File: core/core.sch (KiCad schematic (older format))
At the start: 53 parts, among them J1 Micro_SD_Card, J2 UART_DEBUG, J3 Conn_ARM_JTAG_SWD_10, J4 Conn_01x02, J5 USB_OTG, SW1 RESET, SW2 USER, U1 SC18IS600, U2 AP1509-50, U3 AP1509-33, U4 USBLC6-2SC6

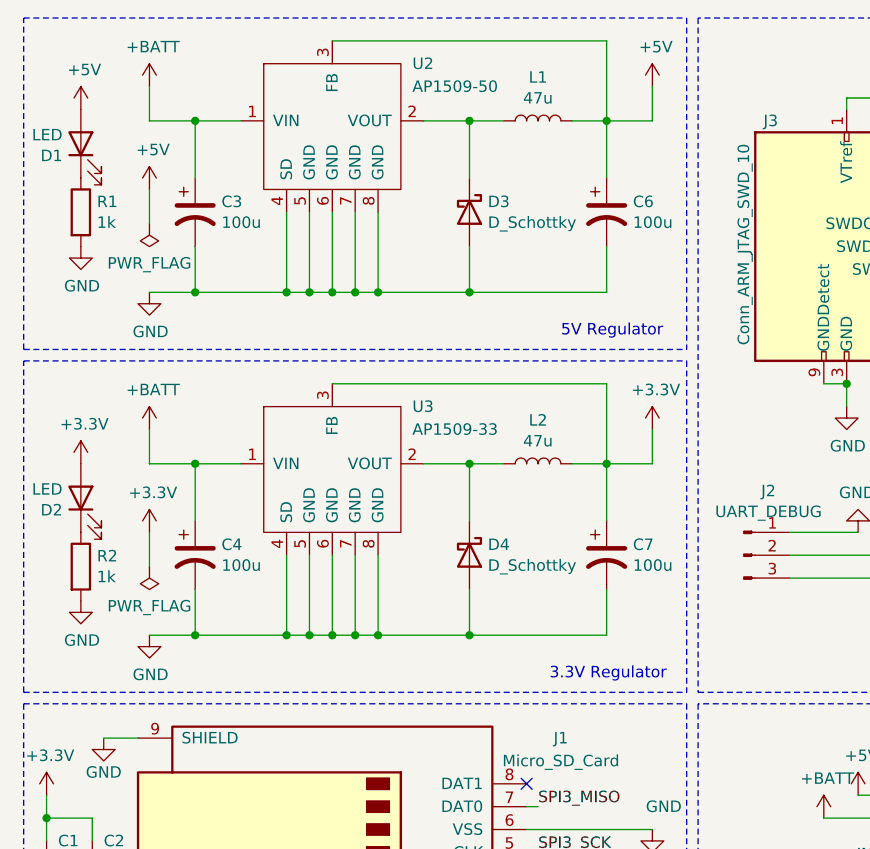
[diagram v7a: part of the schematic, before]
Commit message: New regulator
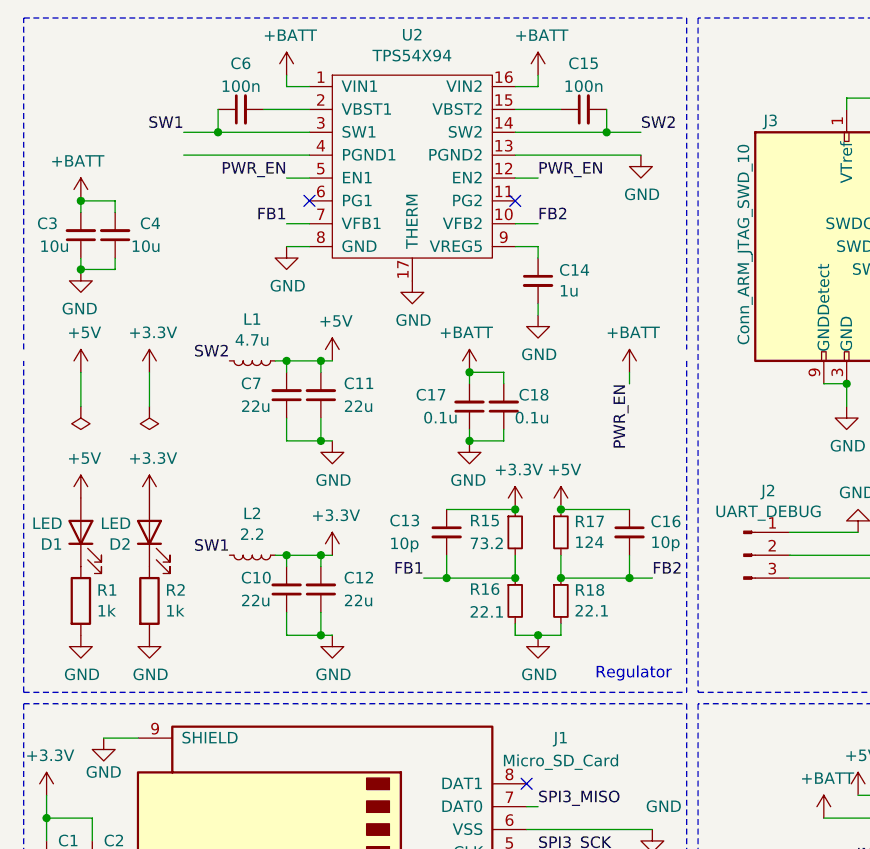
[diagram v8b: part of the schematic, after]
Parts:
- removed C3, C4, C6, C7: 100u, Capacitor_SMD:C_1210_3225Metric, symbol Device:CP1
- removed D3, D4: D_Schottky, Diode_SMD:D_0603_1608Metric, symbol Device:D_Schottky
- removed L1, L2: 47u, Inductor_SMD:L_Bourns-SRN8040_8x8.15mm, symbol Device:L
- removed U2: AP1509-50, Package_SO:SO-8_3.9x4.9mm_P1.27mm, symbol star-common-lib:AP1509-33
- removed U3: AP1509-33, Package_SO:SO-8_3.9x4.9mm_P1.27mm, symbol star-common-lib:AP1509-33
- added C10, C11, C12, C7: 22u, Capacitor_SMD:C_1206_3216Metric, symbol Device:C_Small
- added C13, C16: 10p, Capacitor_SMD:C_1206_3216Metric, symbol Device:C_Small
- added C14: 1u, Capacitor_SMD:C_1206_3216Metric, symbol Device:C_Small
- added C15, C6: 100n, Capacitor_SMD:C_1206_3216Metric, symbol Device:C_Small
- added C17, C18: 0.1u, Capacitor_SMD:C_0603_1608Metric, symbol Device:C_Small
- added C3, C4: 10u, Capacitor_SMD:C_0603_1608Metric, symbol Device:C_Small
- added L1: 4.7u, Inductor_SMD:L_Bourns_SRP5030T, symbol Device:L_Small
- added L2: 2.2, Inductor_SMD:L_Bourns_SRP5030T, symbol Device:L_Small
- added R15: 73.2, Resistor_SMD:R_0603_1608Metric, symbol Device:R_Small
- added R16, R18: 22.1, Resistor_SMD:R_0603_1608Metric, symbol Device:R_Small
- added R17: 124, Resistor_SMD:R_0603_1608Metric, symbol Device:R_Small
- added U2: TPS54X94, Package_SO:TSSOP-16-1EP_4.4x5mm_P0.65mm, symbol star-common-lib:TPS54X94
- U4: DIGIKEY (none) -> 497-5235-1-ND; MANF (none) -> USBLC6-2SC6
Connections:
- net +3V3: now also C10.2, C12.2, C13.1, L2.1, R15.1
- net +5V: now also C11.2, C16.1, C7.2, L1.1, R17.1
- net +BATT: now also C17.2, C18.2, C3.2, C4.2, U2.1 (VIN1), U2.12 (EN2), U2.16 (VIN2), U2.5 (EN1)
- net GND: now also C10.1, C11.1, C12.1, C14.2, C17.1, C18.1, C3.1, C4.1, C7.1, R16.2, R18.2, U2.13 (PGND2), U2.17 (THERM), U2.8 (GND)
- new net: C15.1, U2.15 (VBST2)
- new net: C6.2, U2.2 (VBST1)
- new net: C14.1, U2.9 (VREG5)
- new net FB1: C13.2, R15.2, R16.1, U2.7 (VFB1)
- new net FB2: C16.2, R17.2, R18.1, U2.10 (VFB2)
- new net SW1: C6.1, L2.2, U2.3 (SW1)
- new net SW2: C15.2, L1.2, U2.14 (SW2)
- no-connect marks 17 -> 19
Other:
- note added: "Regulator"
- note removed: "3.3V Regulator"
- note removed: "5V Regulator"
- moved on the sheet: D1, D2, R1, R2
